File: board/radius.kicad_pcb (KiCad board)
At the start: 2 copper layers, 25.4 x 28.6 mm, 11 parts, among them IC1 STM8S003F3P, P1 CONN_01X04, P2 CONN_01X10, U1 CH340G, U2 LM2931AZ-3.3/5.0, Y1 Crystal

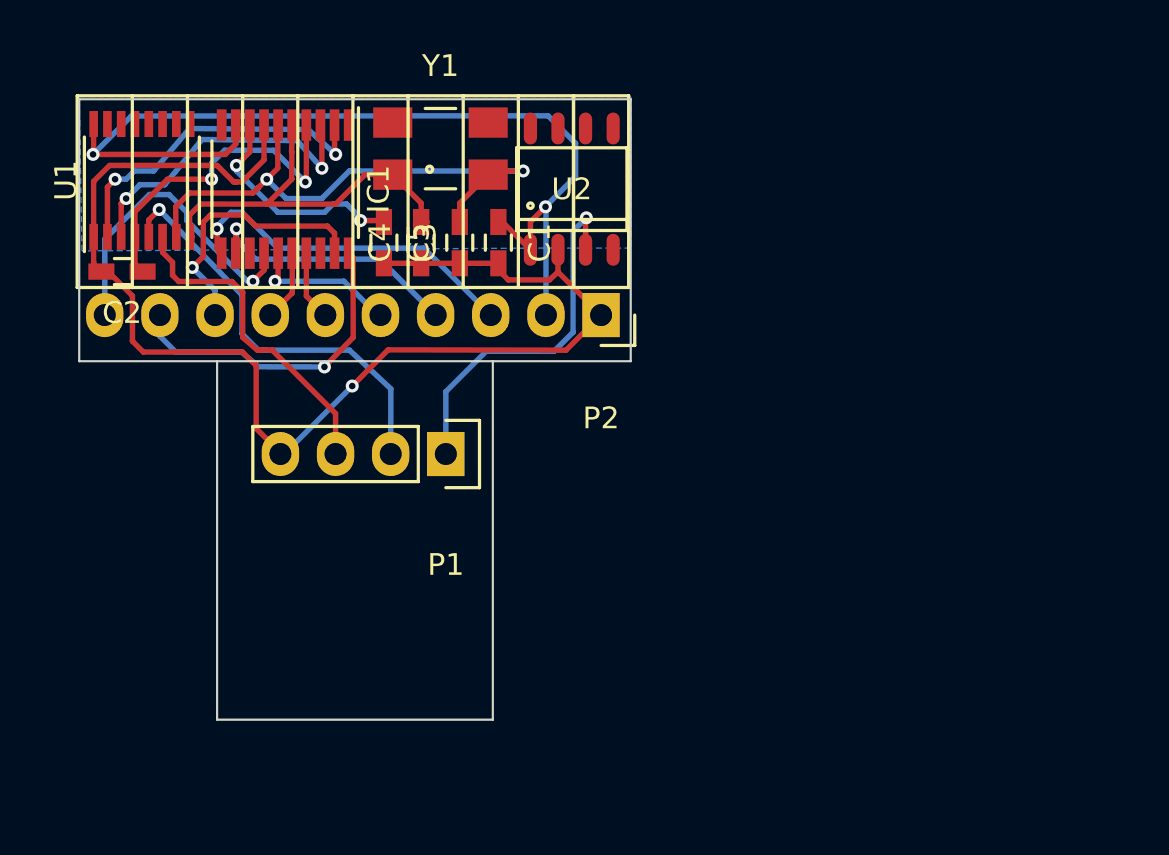
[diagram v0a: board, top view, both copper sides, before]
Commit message: Adds USB connector.
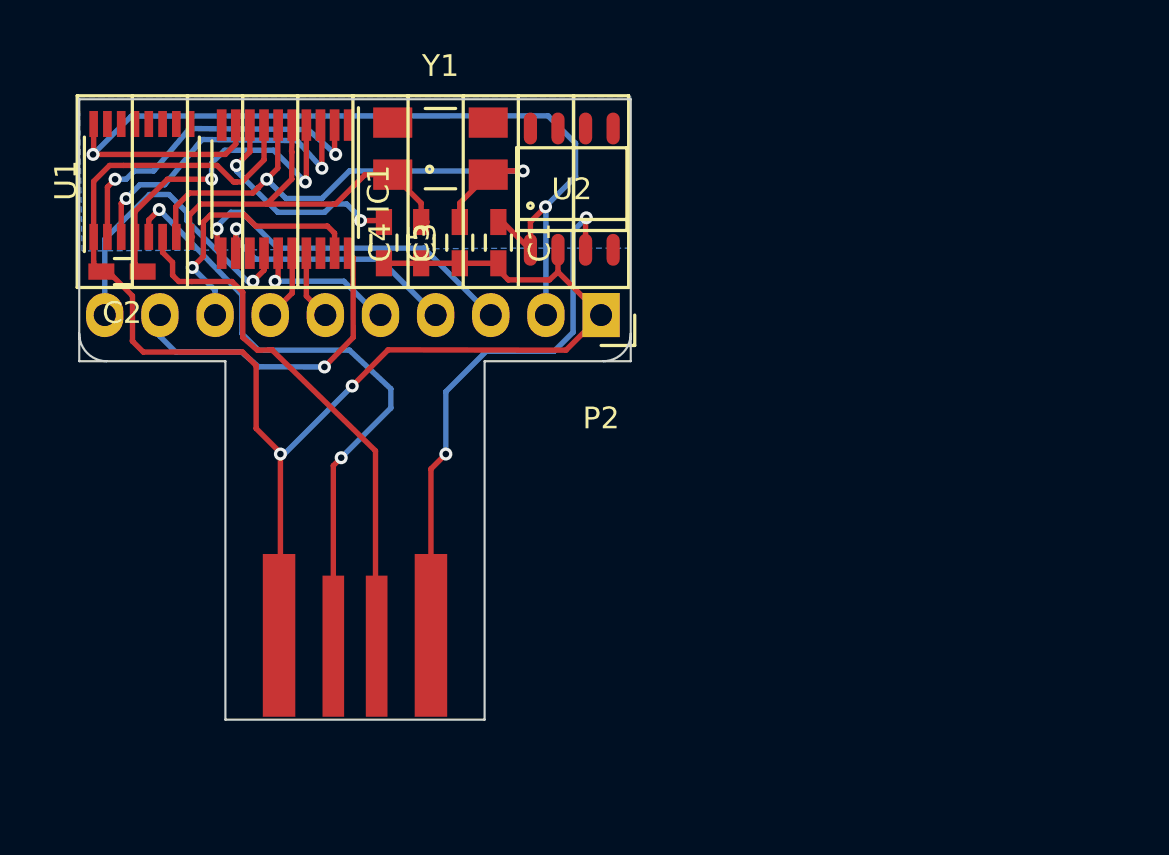
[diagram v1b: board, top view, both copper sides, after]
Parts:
- P1: footprint Socket_Strips:Socket_Strip_Straight_1x04 -> usbpcb:USB-A-PCB
- moved P1 9.52 mm to (145.4, 124.0), turned to 270 degrees
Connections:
- IC1 pad 1: Net-(IC1-Pad1) -> (no net)
- IC1 pad 10: Net-(IC1-Pad10) -> (no net)
- IC1 pad 13: Net-(IC1-Pad13) -> (no net)
- IC1 pad 18: Net-(IC1-Pad18) -> (no net)
- P1 pad 2: D+ -> D-
- P1 pad 3: D- -> D+
- U1 pad 10: Net-(U1-Pad10) -> (no net)
- U1 pad 11: Net-(U1-Pad11) -> (no net)
- U1 pad 12: Net-(U1-Pad12) -> (no net)
- U1 pad 13: Net-(U1-Pad13) -> (no net)
- U1 pad 14: Net-(U1-Pad14) -> (no net)
- U1 pad 15: Net-(U1-Pad15) -> (no net)
- U1 pad 9: Net-(U1-Pad9) -> (no net)
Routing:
- net D+: track 19.6 -> 29.7 mm, vias 1 -> 2
- net D-: track 15.2 -> 24.9 mm
- net GND: track 59.7 -> 68.4 mm, vias 1 -> 2
- net +5V: track 16.9 -> 25.5 mm, vias 1 -> 2
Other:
- outline, holes or cut-outs redrawn

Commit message: Expands footprint of board.
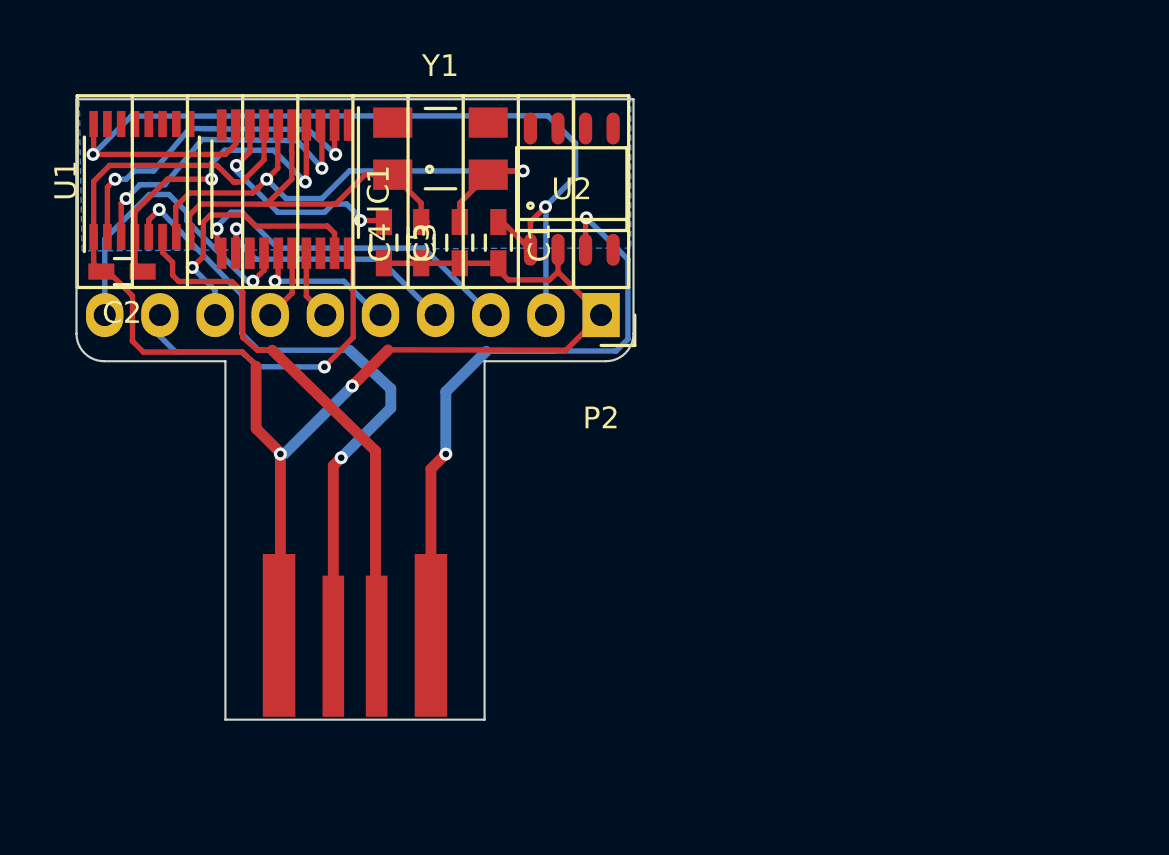
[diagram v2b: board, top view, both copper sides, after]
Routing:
- net +5V: track 25.5 -> 28.8 mm
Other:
- board size 25.4 x 28.6 mm -> 25.7 x 28.6 mm
- net class Wide added: clearance 0.2, trace_width 0.5, via_dia 0.6, via_drill 0.4

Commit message: Corrects footprints for CH340G, start over.
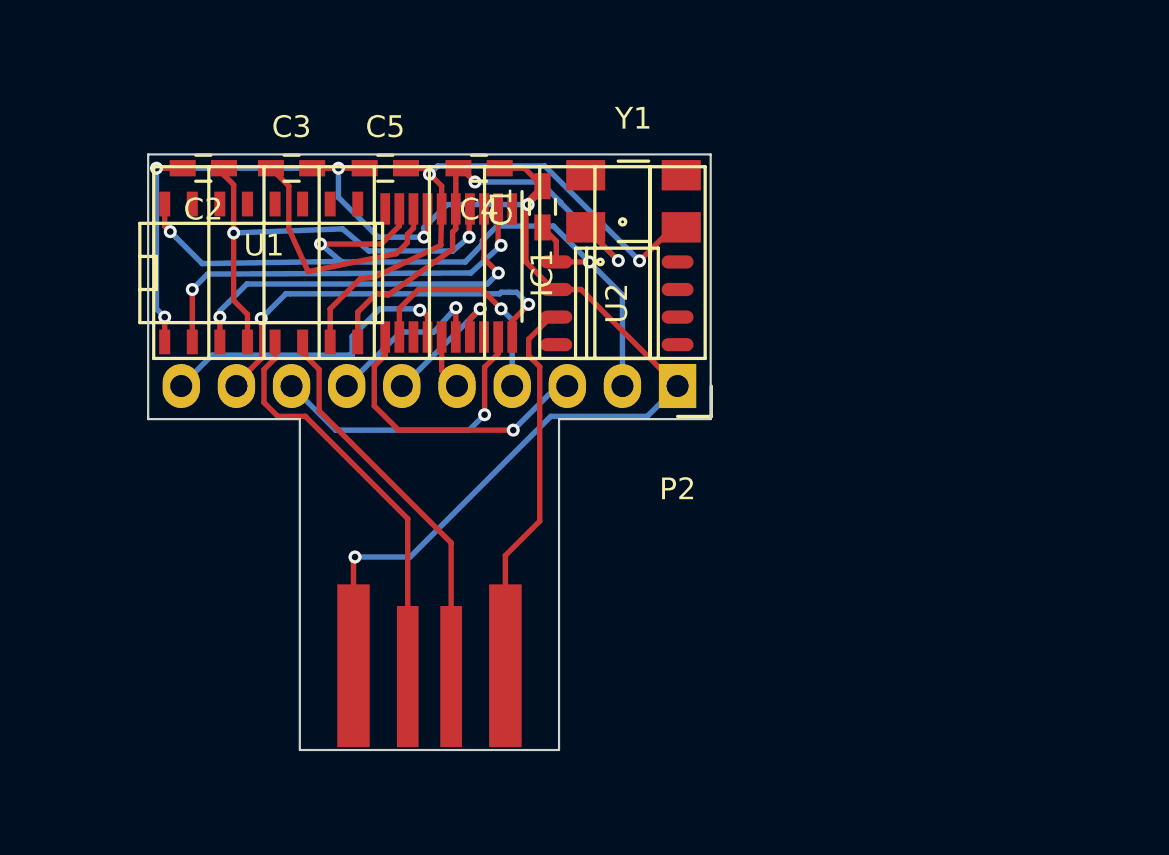
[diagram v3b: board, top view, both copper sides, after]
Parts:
- U1: footprint Housings_SSOP:SSOP-16_3.9x4.9mm_Pitch0.635mm -> SMD_Packages:SO-16-N
- moved Y1 9.21 mm to (158.2, 103.8)
- moved IC1 8.46 mm to (149.7, 107.1)
- moved U1 6.96 mm to (141.1, 107.1), turned to 0 degrees
- moved C2 6.06 mm to (138.4, 102.2)
- moved U2 5.65 mm to (157.5, 108.5), turned to 270 degrees
- moved C3 5.46 mm to (142.5, 102.2), turned to 0 degrees
- moved C5 4.85 mm to (146.8, 102.2), turned to 0 degrees
- moved P2 4.81 mm to (160.3, 112.3)
- moved C4 4.34 mm to (151.1, 102.2), turned to 180 degrees
- moved P1 3.70 mm to (148.8, 125.3)
- moved C1 2.62 mm to (154.1, 104.0), turned to 90 degrees
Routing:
- net +5V: track 28.8 -> 17.6 mm, vias 2 -> 0
- net D+: track 29.7 -> 19.1 mm, vias 2 -> 0
- net VCC: track 45.3 -> 38.5 mm, vias 2 -> 3
- net D-: track 24.9 -> 18.2 mm
- net Net-(C2-Pad1): track 15.7 -> 21.2 mm
- net GND: track 68.4 -> 73.9 mm, vias 2 -> 6
- net MOSI: track 3.27 -> 7.90 mm, vias 0 -> 1
- net SCK: track 7.15 -> 2.55 mm, vias 1 -> 0
- net RXD: track 15.2 -> 18.8 mm, vias 1 -> 2
- net USB_RX: track 14.7 -> 18.2 mm
- net MISO: track 3.21 -> 6.57 mm, vias 0 -> 1
- net USB_TX: track 15.9 -> 19.2 mm
- net XO: track 18.8 -> 21.9 mm, vias 0 -> 2
- net SDA: track 16.3 -> 13.6 mm
- net SCL: track 12.4 -> 10.5 mm
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- removed copper zone on B.Cu, net VCC
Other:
- board size 25.7 x 28.6 mm -> 25.9 x 27.4 mm
- net class Wide removed

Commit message: Thicker traces.
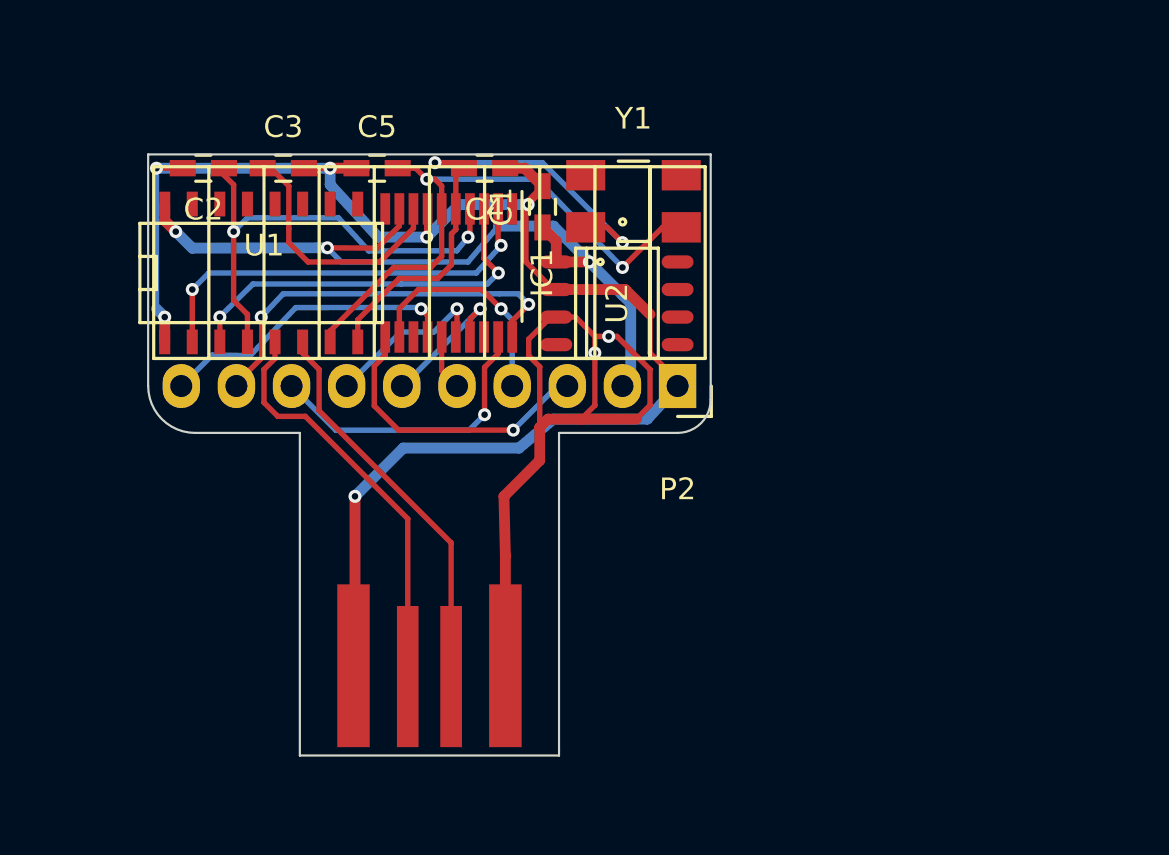
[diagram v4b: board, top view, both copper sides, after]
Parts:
- moved C3 0.38 mm to (142.1, 102.2)
- moved C5 0.38 mm to (146.4, 102.2)
- moved C4 0.25 mm to (151.4, 102.2)
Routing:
- net +5V: track 17.6 -> 34.2 mm, vias 0 -> 2
- net XO: track 21.9 -> 25.0 mm
- net GND: track 73.9 -> 76.1 mm
- net VCC: track 38.5 -> 37.1 mm
- net Net-(C2-Pad1): track 21.2 -> 21.9 mm
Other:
- board size 25.9 x 27.4 mm -> 25.9 x 27.7 mm
- rule trace_min: 0.2 -> 0.1524

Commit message: New alignment.
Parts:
- P1, P2: moved to B.Cu
- moved C2 40.1 mm to (178.4, 105.2), turned to 0 degrees
- moved U1 34.3 mm to (175.3, 109.9)
- moved C3 32.6 mm to (174.6, 105.2), turned to 180 degrees
- moved C5 18.4 mm to (164.6, 105.2)
- moved P1 17.4 mm to (166.2, 126.2)
- moved C4 17.3 mm to (168.4, 105.2)
- moved IC1 16.6 mm to (166.1, 110.0)
- moved C1 8.24 mm to (161.8, 106.8)
- moved P2 5.20 mm to (155.9, 115.1), turned to 0 degrees
- moved U2 2.90 mm to (158.2, 111.3), turned to 90 degrees
- moved Y1 2.84 mm to (157.7, 106.6), turned to 180 degrees
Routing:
- net GND: track 76.1 -> 0.00 mm, vias 6 -> 0
- net VCC: track 37.1 -> 0.00 mm, vias 3 -> 0
- net +5V: track 34.2 -> 0.00 mm, vias 2 -> 0
- net XI: track 27.3 -> 0.00 mm, vias 2 -> 0
- net XO: track 25.0 -> 0.00 mm, vias 2 -> 0
- net Net-(C2-Pad1): track 21.9 -> 0.00 mm, vias 2 -> 0
- net USB_TX: track 19.3 -> 0.00 mm, vias 2 -> 0
- net D+: track 19.1 -> 0.00 mm
- net RXD: track 18.8 -> 0.00 mm, vias 2 -> 0
- net D-: track 18.2 -> 0.00 mm
- net USB_RX: track 18.0 -> 0.00 mm, vias 2 -> 0
- net G3: track 14.3 -> 0.00 mm, vias 1 -> 0
- net TXD: track 13.9 -> 0.00 mm, vias 1 -> 0
- net SDA: track 13.6 -> 0.00 mm, vias 1 -> 0
- net Net-(C3-Pad1): track 11.4 -> 0.00 mm
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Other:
- board outline removed
- rule trace_min: 0.1524 -> 0.2

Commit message: Board edges.
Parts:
- moved P1 2.07 mm to (167.4, 127.9)
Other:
- board outline added: 26.3 x 27.6 mm
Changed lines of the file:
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@@
     (links 35)
     (no_connects 35)
-    (area 0 0 0 0)
+    (area 150.657477 101.618 181.123001 130.225001)
     (thickness 1.6)
-    (drawings 0)
+    (drawings 14)
     (tracks 0)
     (zones 0)
@@
     (zone_45_only no)
     (trace_min 0.2)
-    (segment_width 0.2)
+    (segment_width 0.381)
     (edge_width 0.1)
     (via_size 0.6)
@@
   )
   (module usbpcb:USB-A-PCB (layer B.Cu)
-    (at 166.243 126.1745 270)
+    (at 167.386 127.903 270)
     (descr "Card-edge USB A connector.")
     (fp_text reference P1 (at 0 0 270) (layer Cmts.User) hide
@@
     (pad 4 smd rect (at -2.19964 -1.19888 180) (size 1.80086 1.39954) (layers F.Cu F.Paste F.Mask))
   )
+  (gr_line (start 173.355 116.586) (end 180.467 116.586) (angle 90) (layer Edge.Cuts) (width 0.1))
+  (gr_line (start 173.355 131.826) (end 173.355 116.586) (angle 90) (layer Edge.Cuts) (width 0.1))
+  (gr_line (start 161.417 131.826) (end 173.355 131.826) (angle 90) (layer Edge.Cuts) (width 0.1))
+  (gr_line (start 161.417 116.586) (end 160.274 116.586) (angle 90) (layer Edge.Cuts) (width 0.1))
+  (gr_line (start 161.417 131.826) (end 161.417 116.586) (angle 90) (layer Edge.Cuts) (width 0.1))
+  (gr_line (start 154.178 116.586) (end 154.178 104.267) (angle 90) (layer Edge.Cuts) (width 0.1))
+  (gr_line (start 154.305 116.586) (end 154.178 116.586) (angle 90) (layer Edge.Cuts) (width 0.1))
+  (gr_line (start 160.274 116.586) (end 154.305 116.586) (angle 90) (layer Edge.Cuts) (width 0.1))
+  (gr_line (start 180.467 104.267) (end 180.467 116.586) (angle 90) (layer Edge.Cuts) (width 0.1))
+  (gr_line (start 180.213 104.521) (end 180.213 105.283) (angle 90) (layer Margin) (width 0.381))
+  (gr_line (start 171.958 104.267) (end 180.467 104.267) (angle 90) (layer Edge.Cuts) (width 0.1))
+  (gr_line (start 154.178 104.267) (end 171.958 104.267) (angle 90) (layer Edge.Cuts) (width 0.1))
+  (gr_line (start 154.432 104.521) (end 154.432 107.315) (angle 90) (layer Margin) (width 0.381))
+  (gr_line (start 154.7495 104.4702) (end 164.5285 104.4702) (angle 90) (layer Margin) (width 0.381))
 )

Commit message: Completed edges.
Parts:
- moved C3 1.02 mm to (173.6, 105.2)
- turned C2 to 180 degrees
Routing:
- net GND: track 0.00 -> 76.1 mm, vias 0 -> 6
- net XI: track 0.00 -> 34.9 mm, vias 0 -> 2
- net XO: track 0.00 -> 29.4 mm, vias 0 -> 2
- net D-: track 0.00 -> 25.4 mm, vias 0 -> 1
- net Net-(C2-Pad1): track 0.00 -> 21.8 mm, vias 0 -> 3
- net D+: track 0.00 -> 21.3 mm, vias 0 -> 1
- net VCC: track 0.00 -> 20.9 mm, vias 0 -> 2
- net +5V: track 0.00 -> 19.0 mm, vias 0 -> 1
- net G3: track 0.00 -> 17.4 mm, vias 0 -> 1
- net Net-(C3-Pad1): track 0.00 -> 14.6 mm, vias 0 -> 2
- net USB_RX: track 0.00 -> 10.8 mm, vias 0 -> 2
- net RXD: track 0.00 -> 10.4 mm, vias 0 -> 1
- net TXD: track 0.00 -> 8.87 mm, vias 0 -> 1
- net USB_TX: track 0.00 -> 8.20 mm, vias 0 -> 2
- net MOSI: track 0.00 -> 7.56 mm, vias 0 -> 1
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
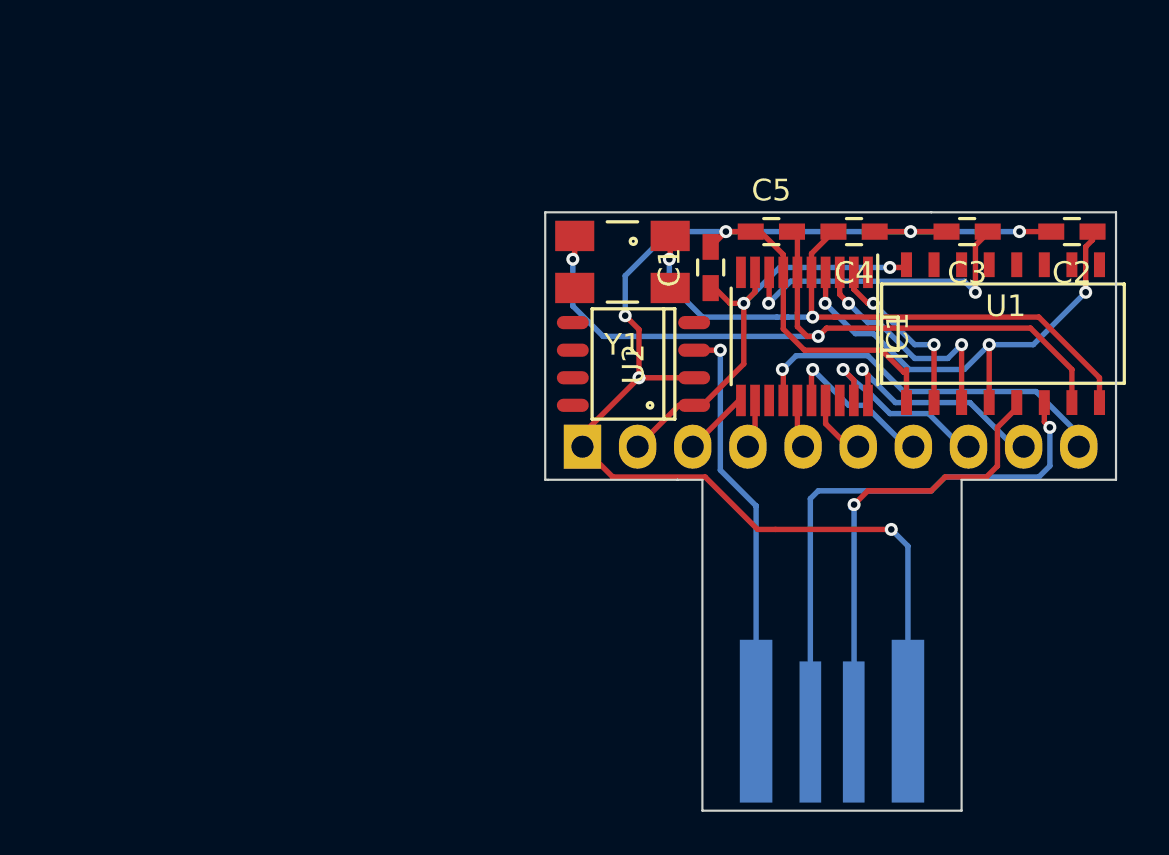
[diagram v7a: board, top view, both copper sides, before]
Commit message: Completes power rails, layout.
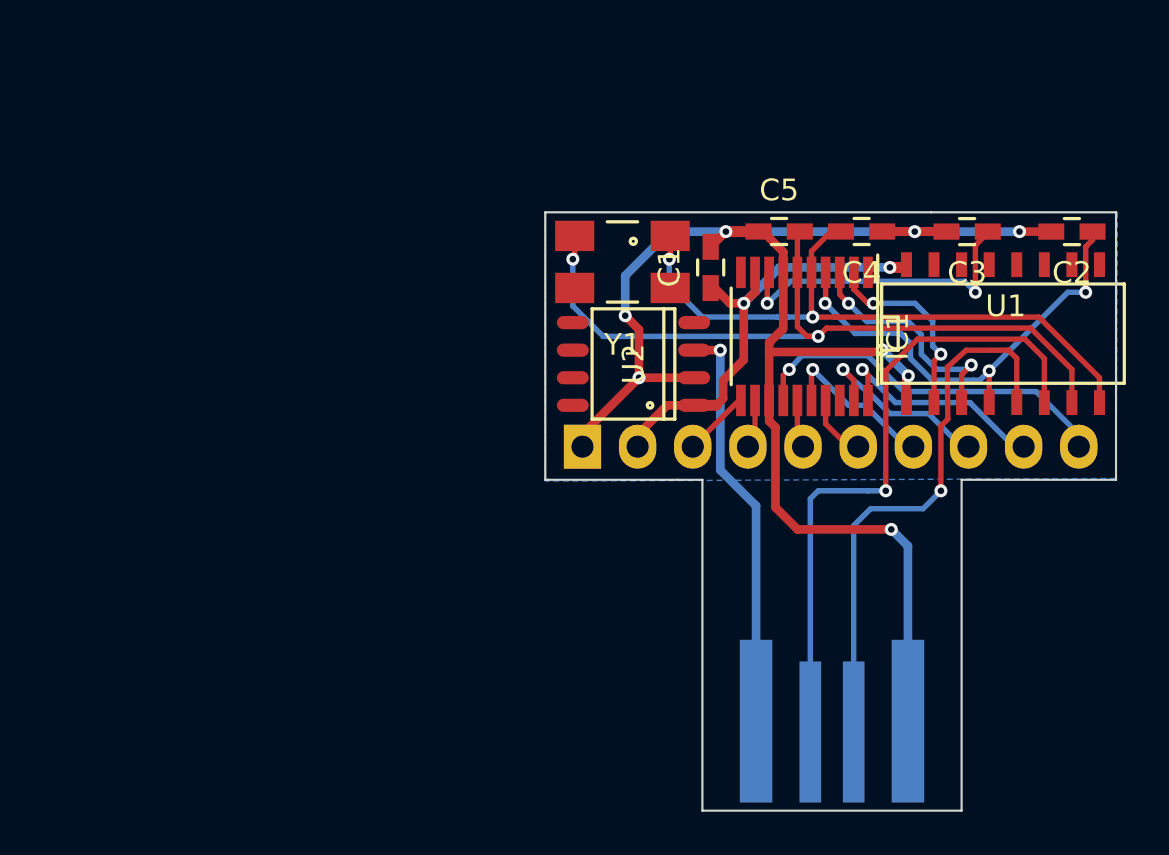
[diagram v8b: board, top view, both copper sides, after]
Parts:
- moved C5 0.36 mm to (164.9, 105.2)
- moved C4 0.35 mm to (168.8, 105.2)
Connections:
- IC1 pad 13: (no net) -> GND
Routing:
- net D-: track 25.4 -> 30.2 mm
- net D+: track 21.3 -> 26.0 mm
- net VCC: track 20.9 -> 22.0 mm
- net GND: track 76.1 -> 75.0 mm, vias 6 -> 8
- net USB_TX: track 8.20 -> 9.06 mm
- added copper zone on B.Cu, net GND
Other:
- net class Power added: clearance 0.2, trace_width 0.4, via_dia 0.6, via_drill 0.4
